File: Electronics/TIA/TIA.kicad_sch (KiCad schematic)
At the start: 4 parts, among them U1 ${SIM.PARAMS}

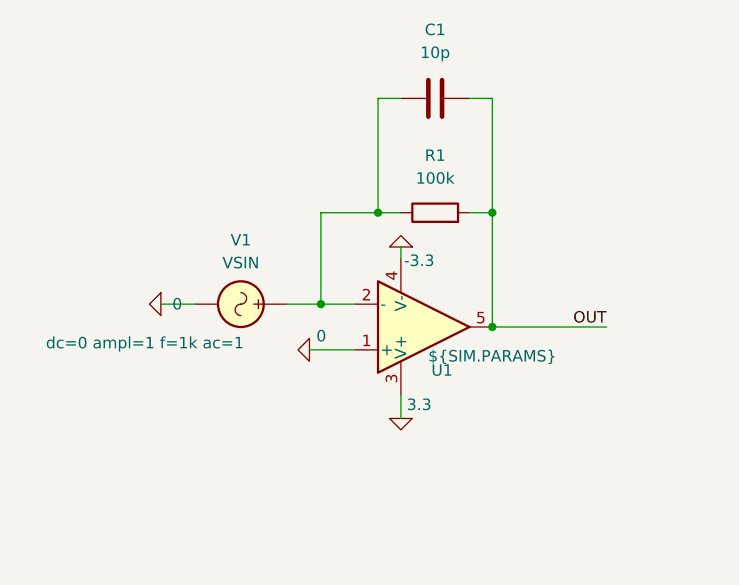
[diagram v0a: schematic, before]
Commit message: Fix TIA simulation
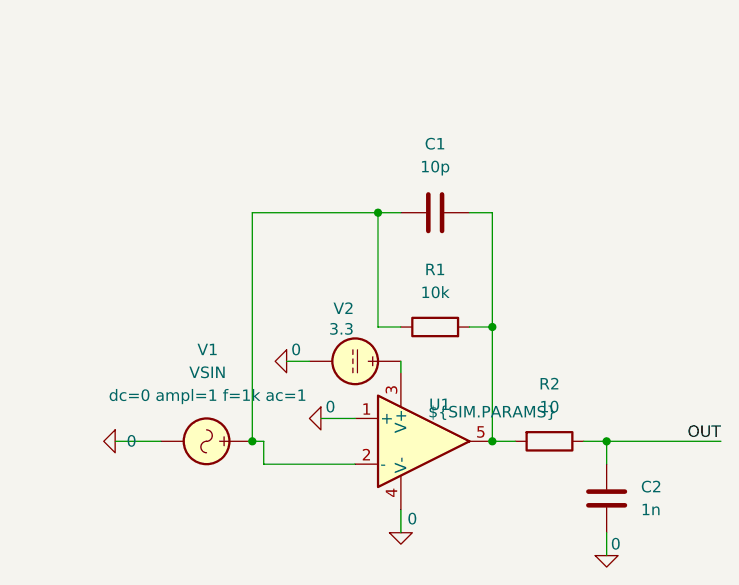
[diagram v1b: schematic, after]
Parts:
- added C2: 1n, symbol Device:C
- added R2: 10, symbol Device:R
- added V2: 3.3, symbol Simulation_SPICE:VDC
- R1: value 100k -> 10k
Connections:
- net -3.3 is gone; now on net 0: U1.4 (V-)
- net 0: now also C2.2, V2.2
- net OUT: now also C2.1, R2.1; no longer C1.2, R1.2, U1.5
- net 3.3: no longer names the net of U1.3 (V+)
- net 3.3: now also V2.1
- new net: C1.2, R1.2, R2.2, U1.5

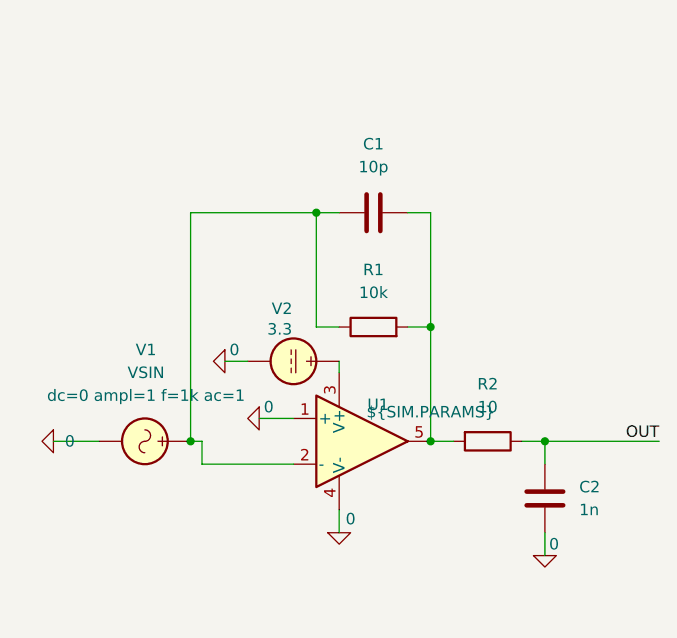
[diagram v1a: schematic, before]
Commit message: Replace voltage source by current source
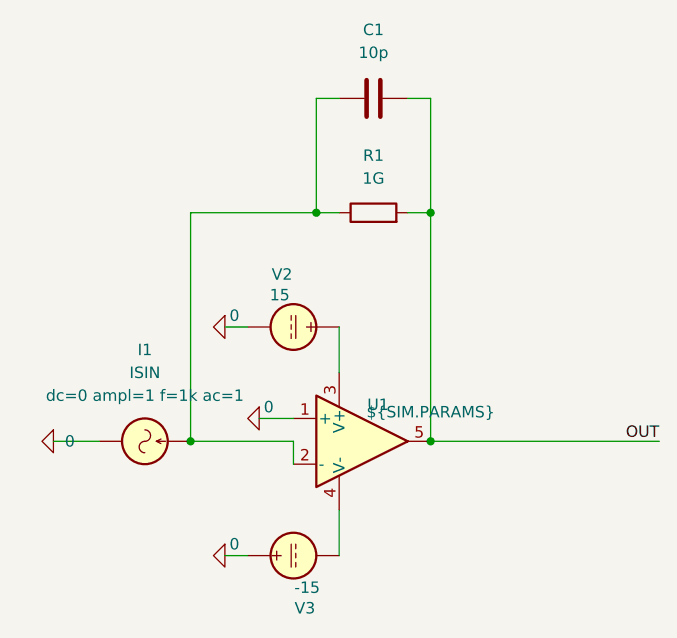
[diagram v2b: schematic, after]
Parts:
- removed C2: 1n, symbol Device:C
- removed R2: 10, symbol Device:R
- removed V1: VSIN, symbol Simulation_SPICE:VSIN
- added I1: ISIN, symbol Simulation_SPICE:ISIN
- added V3: -15, symbol Simulation_SPICE:VDC
- R1: value 10k -> 1G
- V2: value 3.3 -> 15
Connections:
- net 0: now also I1.2, V3.1; no longer U1.4 (V-)
- net OUT: now also C1.2, R1.2, U1.5
- net at C1.1, R1.1, U1.2 (-): now also I1.1
- new net: U1.4 (V-), V3.2
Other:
- moved on the sheet: R1, V2

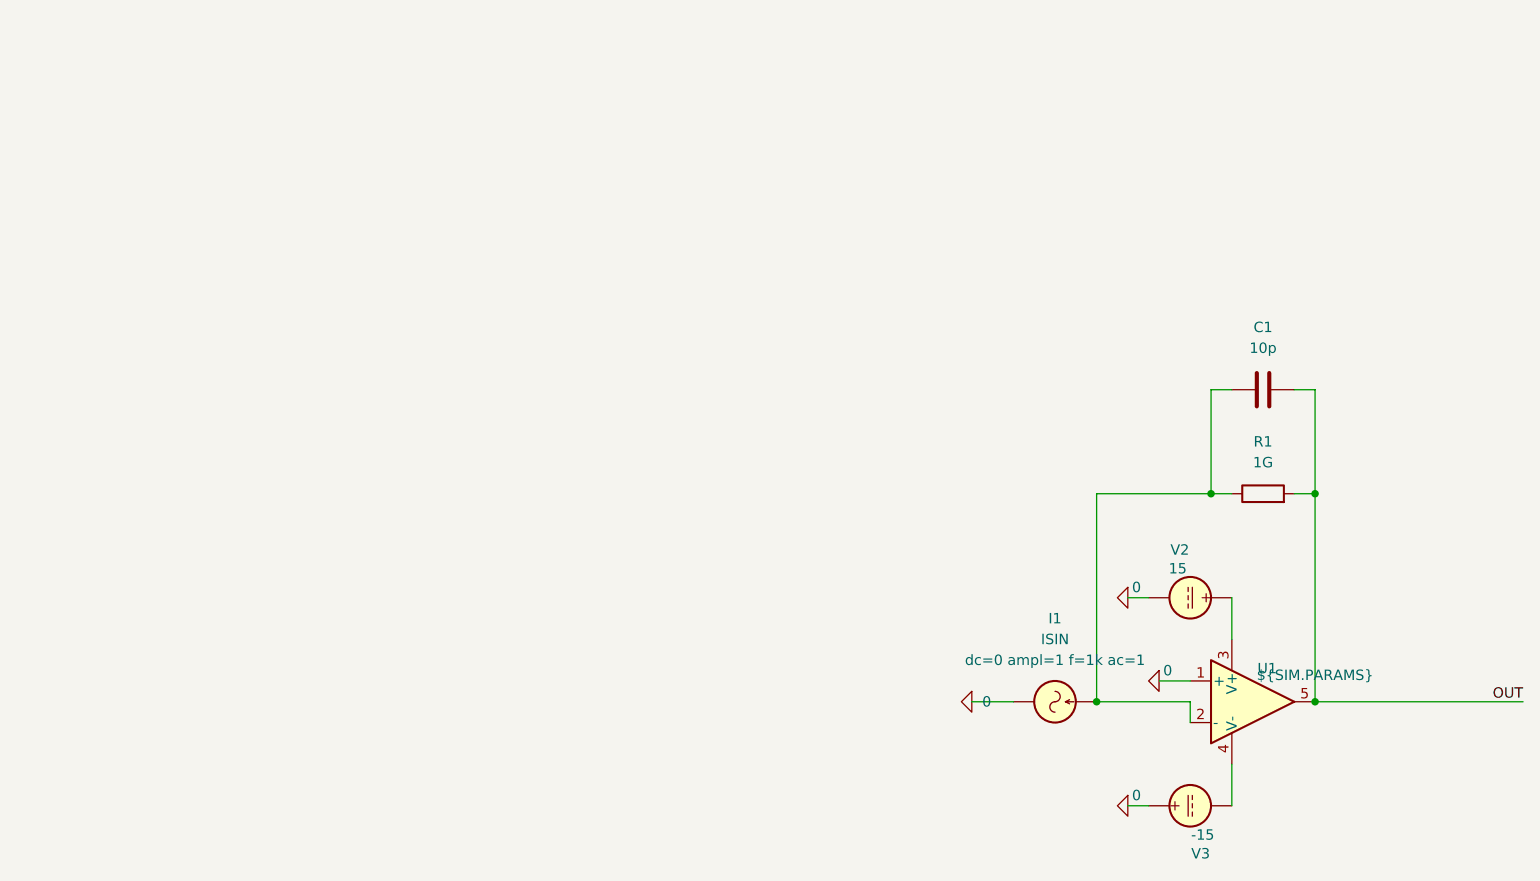
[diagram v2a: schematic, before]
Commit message: Create example of tuned TIA with simulation
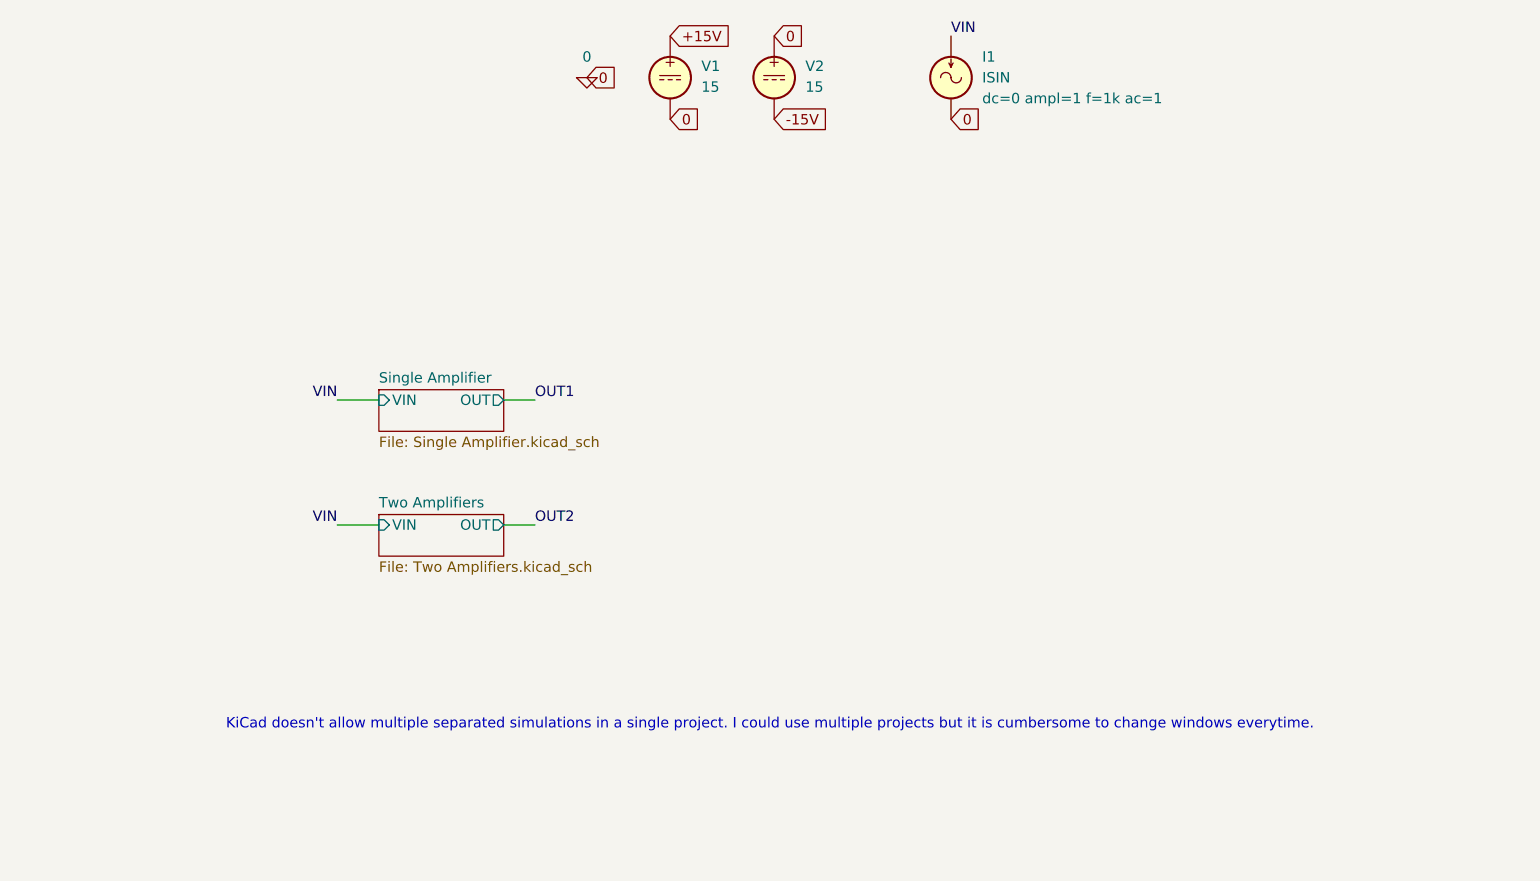
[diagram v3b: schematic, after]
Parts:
- removed C1: 10p, symbol Device:C
- removed R1: 1G, symbol Device:R
- removed U1: ${SIM.PARAMS}, symbol Simulation_SPICE:OPAMP
- removed V3: -15, symbol Simulation_SPICE:VDC
- added V1: 15, symbol Simulation_SPICE:VDC
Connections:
- net 0: now also V2.1, V1.2; no longer V2.2
- net VIN: now reaches I1.1
- new net +15V: V1.1
- new net -15V: V2.2
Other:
- added sheet Single Amplifier (Single Amplifier.kicad_sch)
- added sheet Two Amplifiers (Two Amplifiers.kicad_sch)
- note added: "KiCad doesn't allow multiple separated simulations in a single project. I could use multiple projects but it is cumbersome to change windows everytime."
